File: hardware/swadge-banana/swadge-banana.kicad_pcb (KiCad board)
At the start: 2 copper layers, 85 x 173.2 mm, 48 parts, among them J1 USB_B_Micro, SW1 SW_SPDT, U1 AP1117-33, U2 ESP-13-WROOM-02D, U3 BUS_PCIexpress, U4 OLED_CONNECTOR, U5 QMA6981, U6 OLED_DISPLAY

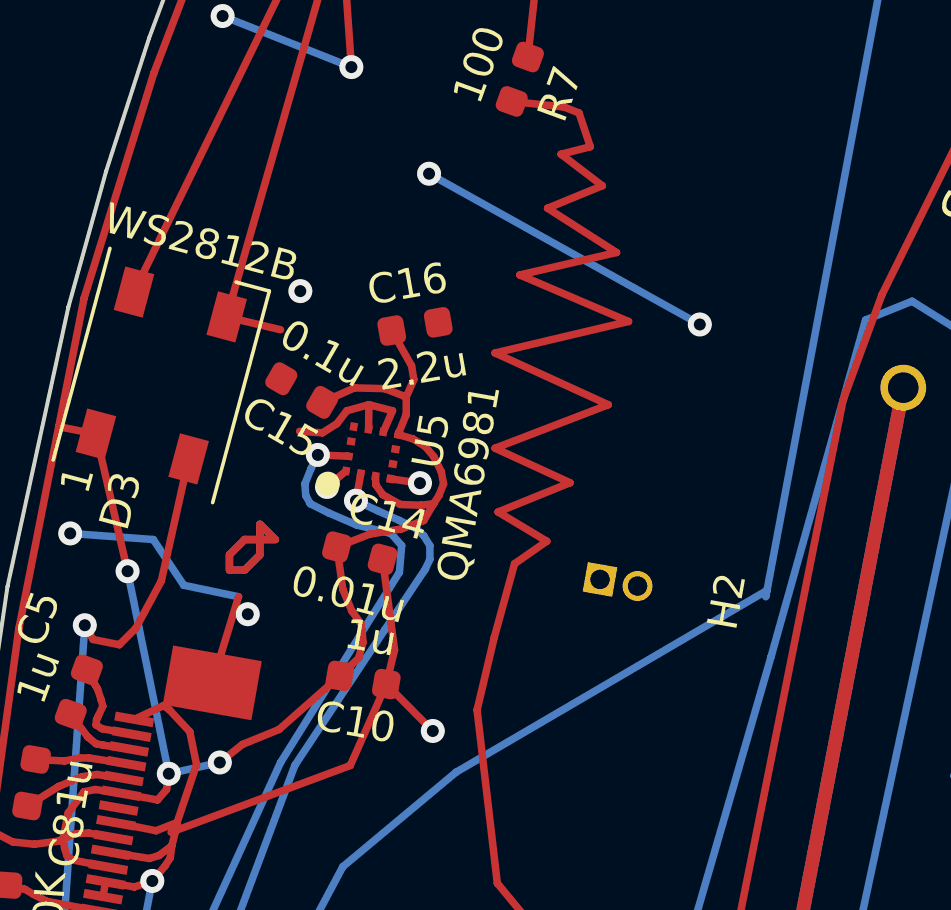
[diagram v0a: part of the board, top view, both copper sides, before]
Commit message: Added series I2C resistors to QMA6981 (Banana)
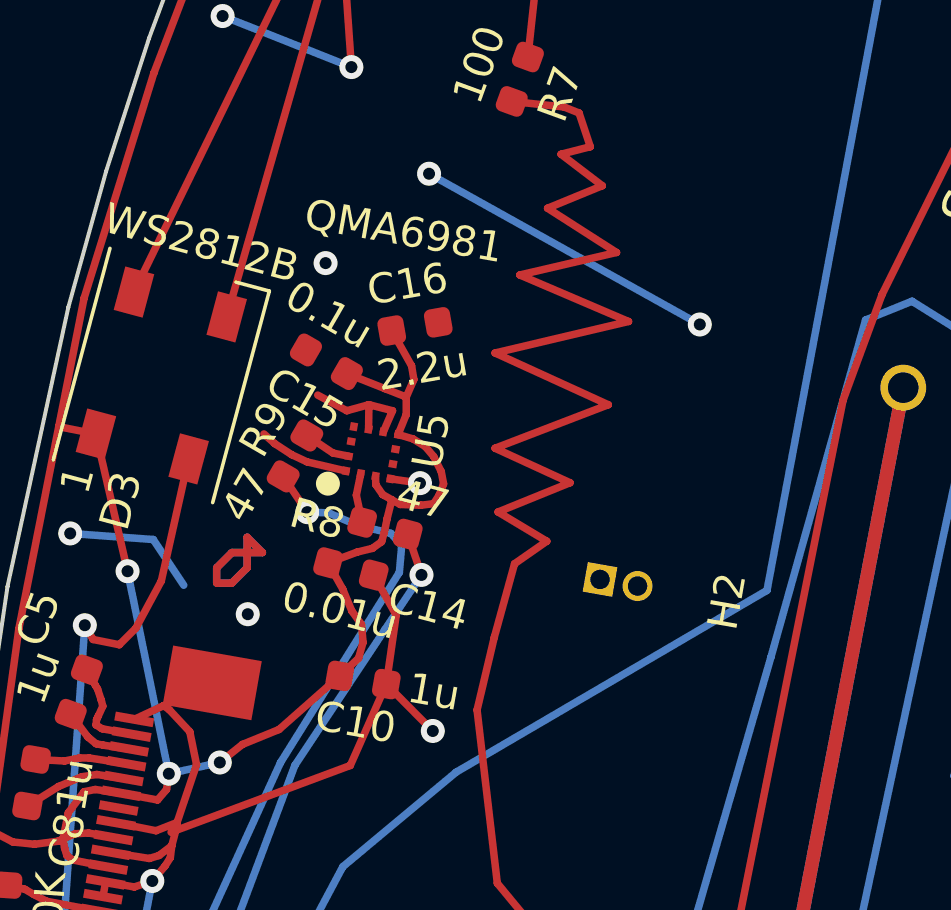
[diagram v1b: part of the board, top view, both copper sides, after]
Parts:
- added R8: 47, Swadge_Parts:R_0603_1608Metric, F.Cu at (124.1, 86.5)
- added R9: 47, Swadge_Parts:R_0603_1608Metric, F.Cu at (121.1, 84.1)
- moved C15 1.26 mm to (122.1, 80.9)
- moved C14 0.61 mm to (122.9, 87.9)
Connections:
- U5 pad 12: SCL -> Net-(R9-Pad2)
- U5 pad 2: SDA -> Net-(R8-Pad1)
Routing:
- net GND: track 669.6 -> 664.0 mm, vias 45 -> 44
- net SDA: track 150.4 -> 146.9 mm
- net Net-(R8-Pad1): track 0.00 -> 1.65 mm
- net Net-(R9-Pad2): track 0.00 -> 1.58 mm
- net +3V3: track 619.3 -> 617.8 mm
- net SCL: track 125.7 -> 124.4 mm
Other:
- board text added: "Swadge 2020 Banana revC"
- board text removed: "Swadge 2020 Banana revB"

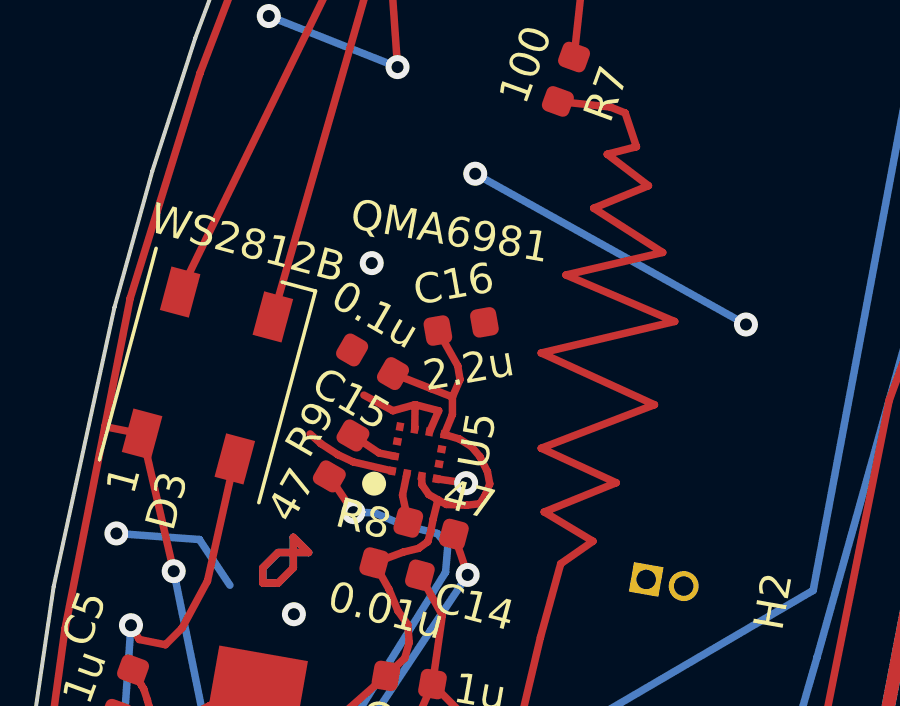
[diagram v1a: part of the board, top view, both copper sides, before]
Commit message: Added new QMA6981 part with larger pads Updated banana and barrel with new pads
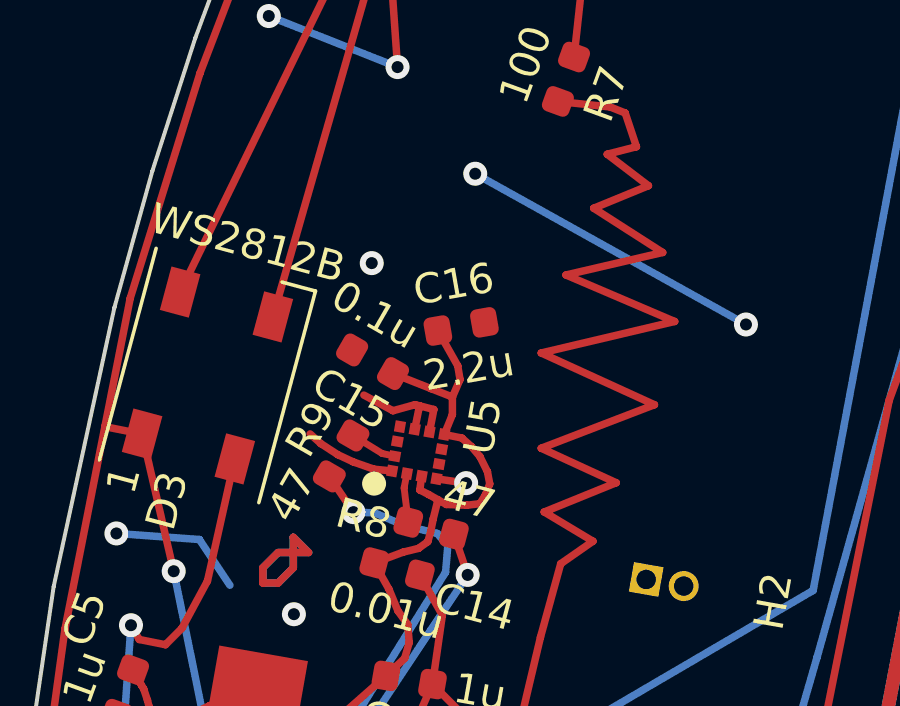
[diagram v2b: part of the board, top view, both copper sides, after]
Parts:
- U5: footprint Swadge_Parts:QMA6981 -> Swadge_Parts:QMA6981_2
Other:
- board text added: "Swadge 2020 Banana revD"
- board text removed: "Swadge 2020 Banana revC"

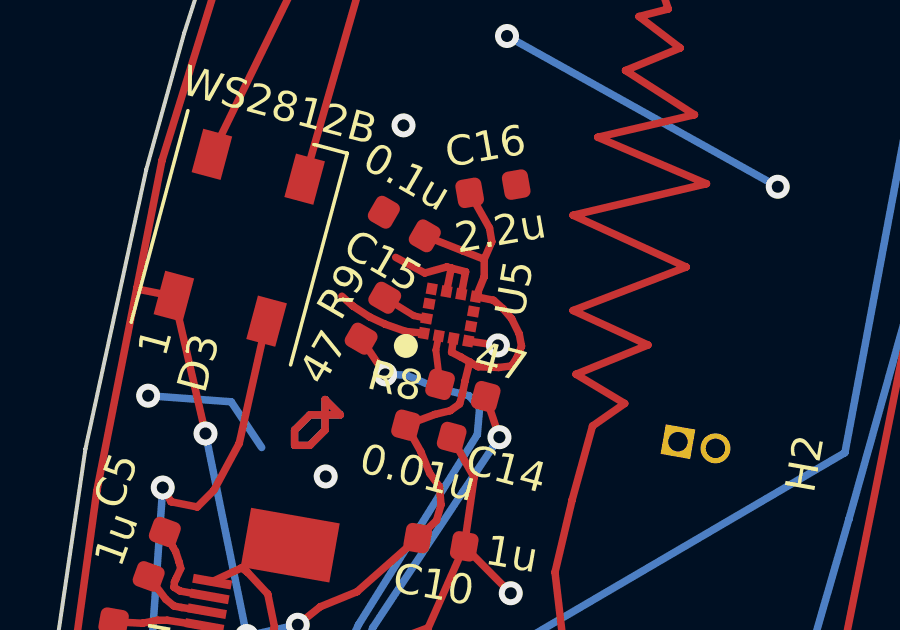
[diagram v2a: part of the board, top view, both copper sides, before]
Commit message: Resized QMA6981_2 pads to 0.3mm x 0.3mm
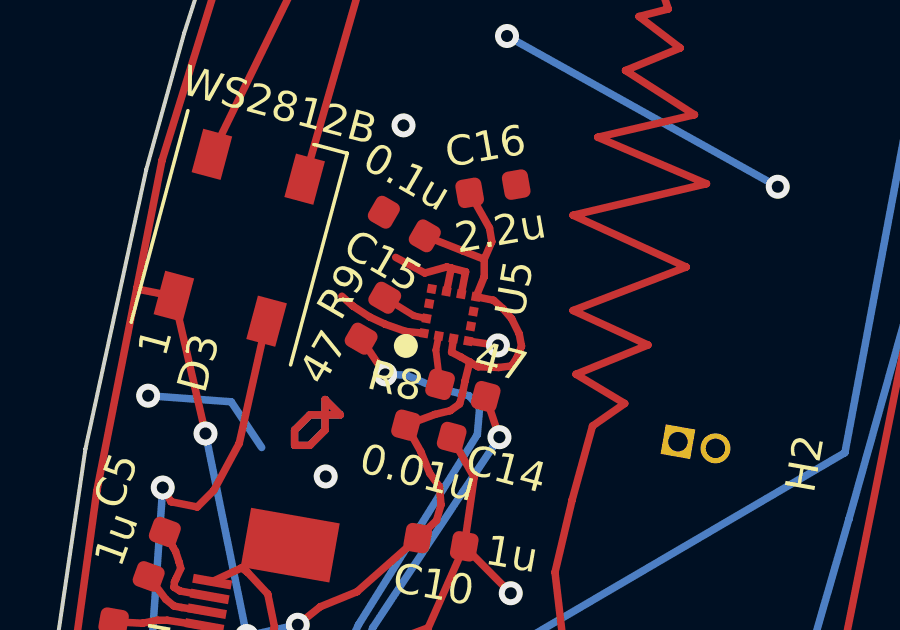
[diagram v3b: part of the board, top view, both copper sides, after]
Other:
- board text added: "Swadge 2020 Banana revE"
- board text removed: "Swadge 2020 Banana revD"
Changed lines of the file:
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@@
   )
   (setup
-    (last_trace_width 0.23)
+    (last_trace_width 0.25)
     (user_trace_width 0.2)
     (user_trace_width 0.22)
@@
     (fp_poly (pts (xy 1.053 1.053) (xy 1.053 -1.053) (xy 0.473 -1.053) (xy 0.473 1.053)) (layer F.Mask) (width 0.001))
     (fp_circle (center -1.27 -1.27) (end -1.07 -1.27) (layer F.SilkS) (width 0.4))
-    (pad 11 smd rect (at 0.25 -0.75 170) (size 0.376 0.35) (layers F.Cu F.Paste F.Mask))
-    (pad 12 smd rect (at -0.25 -0.75 170) (size 0.376 0.35) (layers F.Cu F.Paste F.Mask)
+    (pad 11 smd rect (at 0.25 -0.75 170) (size 0.3 0.3) (layers F.Cu F.Paste F.Mask))
+    (pad 12 smd rect (at -0.25 -0.75 170) (size 0.3 0.3) (layers F.Cu F.Paste F.Mask)
       (net 40 "Net-(R9-Pad2)"))
-    (pad 6 smd rect (at 0.25 0.75 170) (size 0.376 0.35) (layers F.Cu F.Paste F.Mask))
-    (pad 5 smd rect (at -0.25 0.75 170) (size 0.376 0.35) (layers F.Cu F.Paste F.Mask))
-    (pad 8 smd rect (at 0.75 0.25 80) (size 0.376 0.35) (layers F.Cu F.Paste F.Mask)
+    (pad 6 smd rect (at 0.25 0.75 170) (size 0.3 0.3) (layers F.Cu F.Paste F.Mask))
+    (pad 5 smd rect (at -0.25 0.75 170) (size 0.3 0.3) (layers F.Cu F.Paste F.Mask))
+    (pad 8 smd rect (at 0.75 0.25 80) (size 0.3 0.3) (layers F.Cu F.Paste F.Mask)
       (net 31 GND))
-    (pad 9 smd rect (at 0.75 -0.25 80) (size 0.376 0.35) (layers F.Cu F.Paste F.Mask)
+    (pad 9 smd rect (at 0.75 -0.25 80) (size 0.3 0.3) (layers F.Cu F.Paste F.Mask)
       (net 31 GND))
-    (pad 7 smd rect (at 0.75 0.75 80) (size 0.376 0.35) (layers F.Cu F.Paste F.Mask)
+    (pad 7 smd rect (at 0.75 0.75 80) (size 0.3 0.3) (layers F.Cu F.Paste F.Mask)
       (net 32 +3V3))
-    (pad 10 smd rect (at 0.75 -0.75 80) (size 0.376 0.35) (layers F.Cu F.Paste F.Mask))
-    (pad 4 smd rect (at -0.75 0.75 80) (size 0.376 0.35) (layers F.Cu F.Paste F.Mask)
+    (pad 10 smd rect (at 0.75 -0.75 80) (size 0.3 0.3) (layers F.Cu F.Paste F.Mask))
+    (pad 4 smd rect (at -0.75 0.75 80) (size 0.3 0.3) (layers F.Cu F.Paste F.Mask)
       (net 31 GND))
-    (pad 3 smd rect (at -0.75 0.25 80) (size 0.376 0.35) (layers F.Cu F.Paste F.Mask)
+    (pad 3 smd rect (at -0.75 0.25 80) (size 0.3 0.3) (layers F.Cu F.Paste F.Mask)
       (net 32 +3V3))
-    (pad 2 smd rect (at -0.75 -0.25 80) (size 0.376 0.35) (layers F.Cu F.Paste F.Mask)
+    (pad 2 smd rect (at -0.75 -0.25 80) (size 0.3 0.3) (layers F.Cu F.Paste F.Mask)
       (net 39 "Net-(R8-Pad1)"))
-    (pad 1 smd rect (at -0.75 -0.75 80) (size 0.376 0.35) (layers F.Cu F.Paste F.Mask)
+    (pad 1 smd rect (at -0.75 -0.75 80) (size 0.3 0.3) (layers F.Cu F.Paste F.Mask)
       (net 31 GND))
     (model D:/git/Swadge-Devkit/hardware/kicad-libs/package3d/LGA-12_2x2mm_P0.5mm.wrl
@@
     (effects (font (size 2 2) (thickness 0.3)))
   )
-  (gr_text "Swadge 2020\nBanana revD" (at 136.15 48.95 62) (layer B.SilkS)
+  (gr_text "Swadge 2020\nBanana revE" (at 136.15 48.95 62) (layer B.SilkS)
     (effects (font (size 2 2) (thickness 0.3)) (justify mirror))
   )
